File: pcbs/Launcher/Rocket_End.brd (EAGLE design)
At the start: 100 x 80 mm, 28 parts, among them IC1 7805TV, K4 LD105, K5 LD105, K6 LD105, K7 LD105, T1 BC547, T2 BC547, T3 BC547, T4 BC547, T5 BC547, U1 ARDUINO-MEGAPRO-5V, X1 22-23-2041, X2 22-23-2041, X4 22-23-2021, X5 22-23-2021, X6 22-23-2021

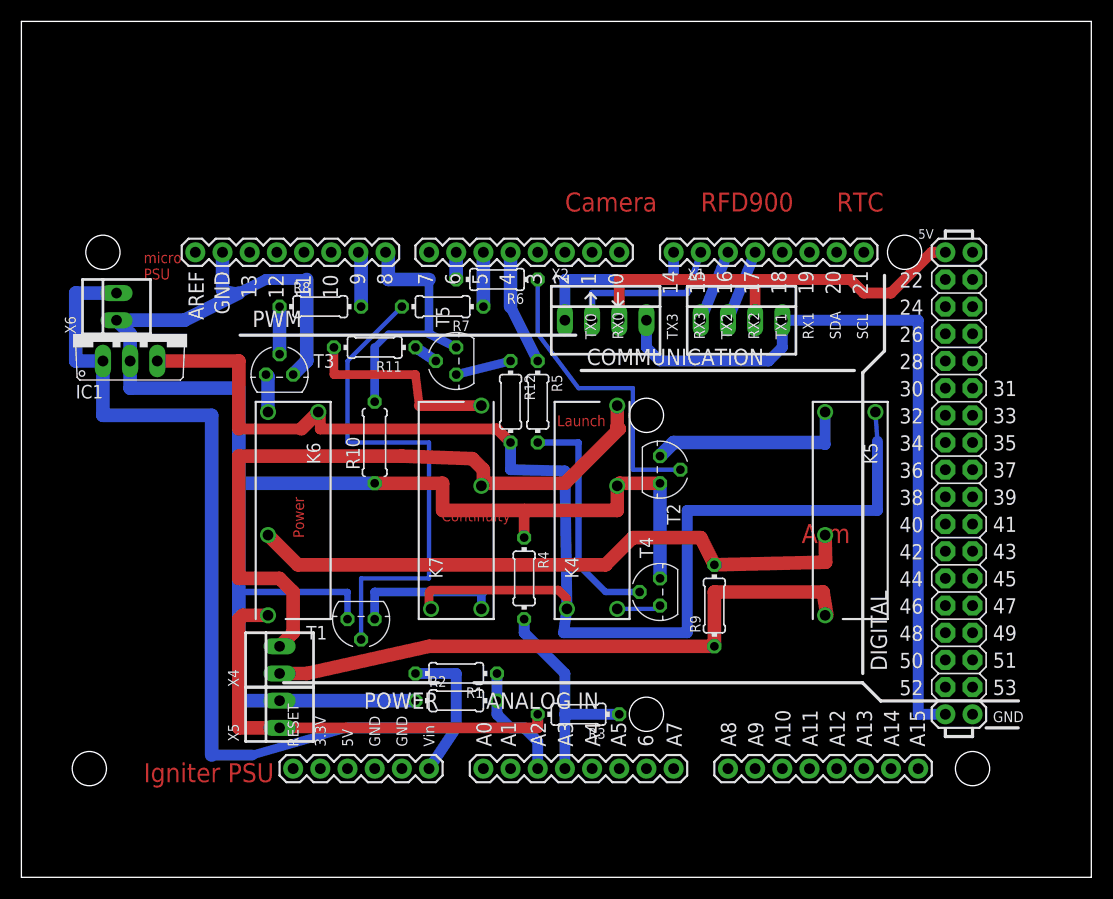
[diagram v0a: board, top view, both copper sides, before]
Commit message: * Much better placement of components and tracks for Rocket_End * Put IMU on bottom of the Sensor board
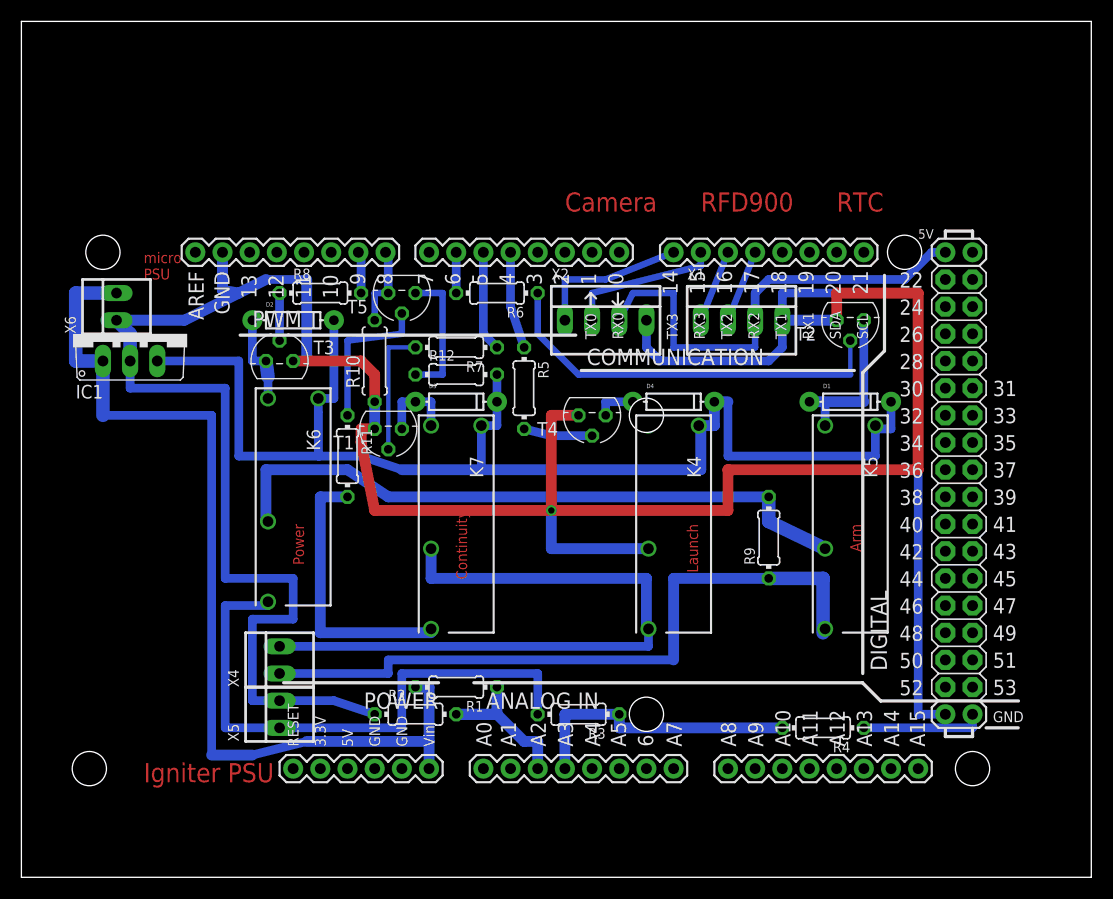
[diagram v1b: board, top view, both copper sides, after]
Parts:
- added D1, D2, D3, D4: (no value), SparkFun-DiscreteSemi:DIODE-1N4148
- moved R4 31.2 mm to (74.9, 14.0), turned to 180 degrees
- moved T2 22.6 mm to (77.5, 52.1), turned to 180 degrees
- moved T1 18.0 mm to (34.3, 41.9)
- moved T4 17.7 mm to (53.3, 43.2), turned to 180 degrees
- moved R11 10.5 mm to (30.5, 39.4), turned to 270 degrees
- moved R9 8.13 mm to (69.8, 31.8)
- moved T5 8.13 mm to (35.6, 54.6), turned to 180 degrees
- moved K4 7.73 mm to (61.0, 33.0), turned to 270 degrees
- moved R10 7.62 mm to (33.0, 48.3)
- moved R12 5.68 mm to (40.6, 47.0), turned to 0 degrees
- moved R7 4.02 mm to (40.6, 49.5)
- moved R2 4.02 mm to (36.8, 15.2)
- moved R5 1.80 mm to (47.0, 45.7)
- moved K6 1.27 mm to (25.4, 35.6)
- moved R6 1.27 mm to (44.5, 54.6)
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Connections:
- new net N$24: R4.1, U1.GND@3
- net GND: no longer R4.1
- net N$19: now also D4.A
- net N$20: now also D3.A
- net N$21: now also D2.A
- net N$22: now also D1.A
- net N$5: now also D1.C, D2.C, D3.C, D4.C
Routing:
- net GND: track 164.4 -> 233.4 mm
- net N$13: track 47.2 -> 12.1 mm
- net N$26: track 25.1 -> 7.87 mm
- net N$12: track 22.0 -> 6.43 mm
- net N$31: track 2.29 -> 14.0 mm
- net N$29: track 42.2 -> 53.9 mm
- net N$24: track 0.00 -> 11.4 mm
- net N$10: track 28.6 -> 37.8 mm
- net N$23: track 5.24 -> 12.7 mm
- net VCC: track 96.4 -> 89.1 mm
- net N$30: track 18.9 -> 25.9 mm
- net N$20: track 14.4 -> 7.50 mm
- net N$17: track 58.4 -> 64.8 mm
- net N$7: track 11.2 -> 17.6 mm
- net N$3: track 20.6 -> 26.7 mm
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
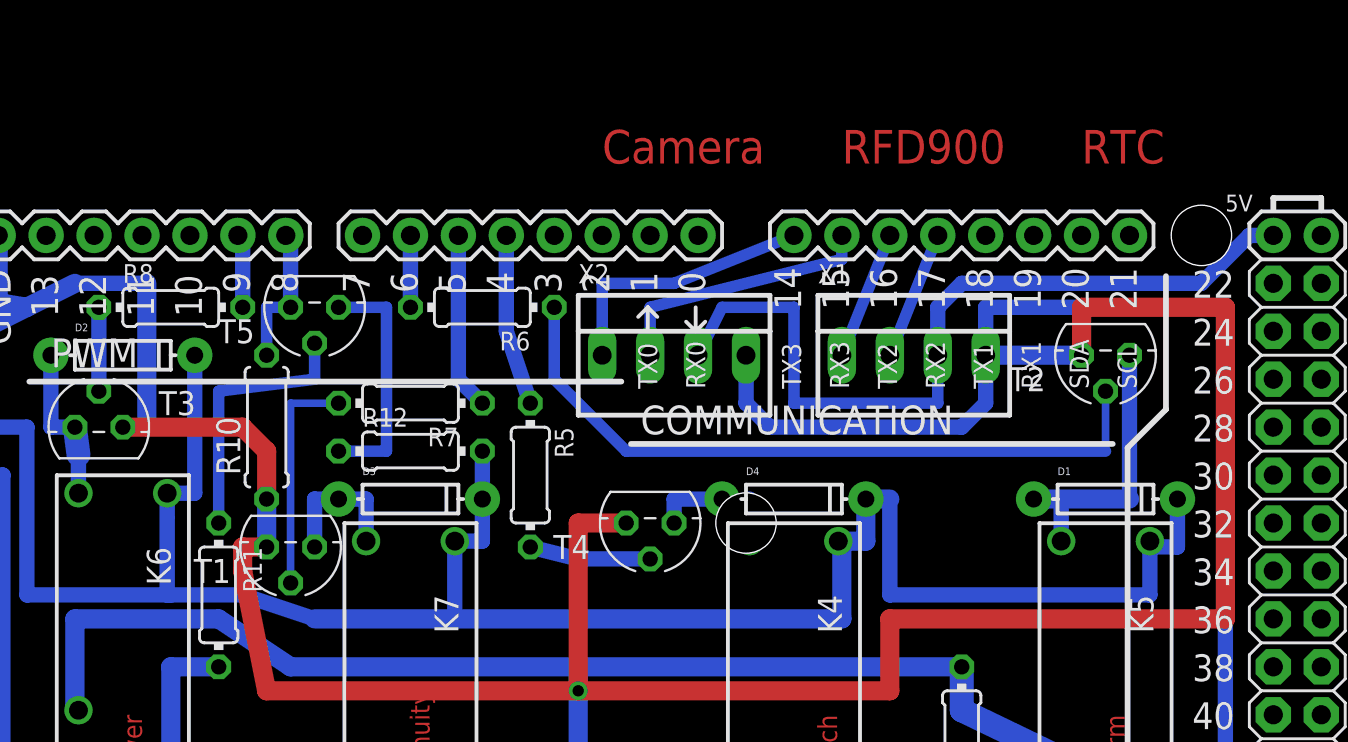
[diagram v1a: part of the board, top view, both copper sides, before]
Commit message: * Using Via to ensure soldering is done on correct side of board.
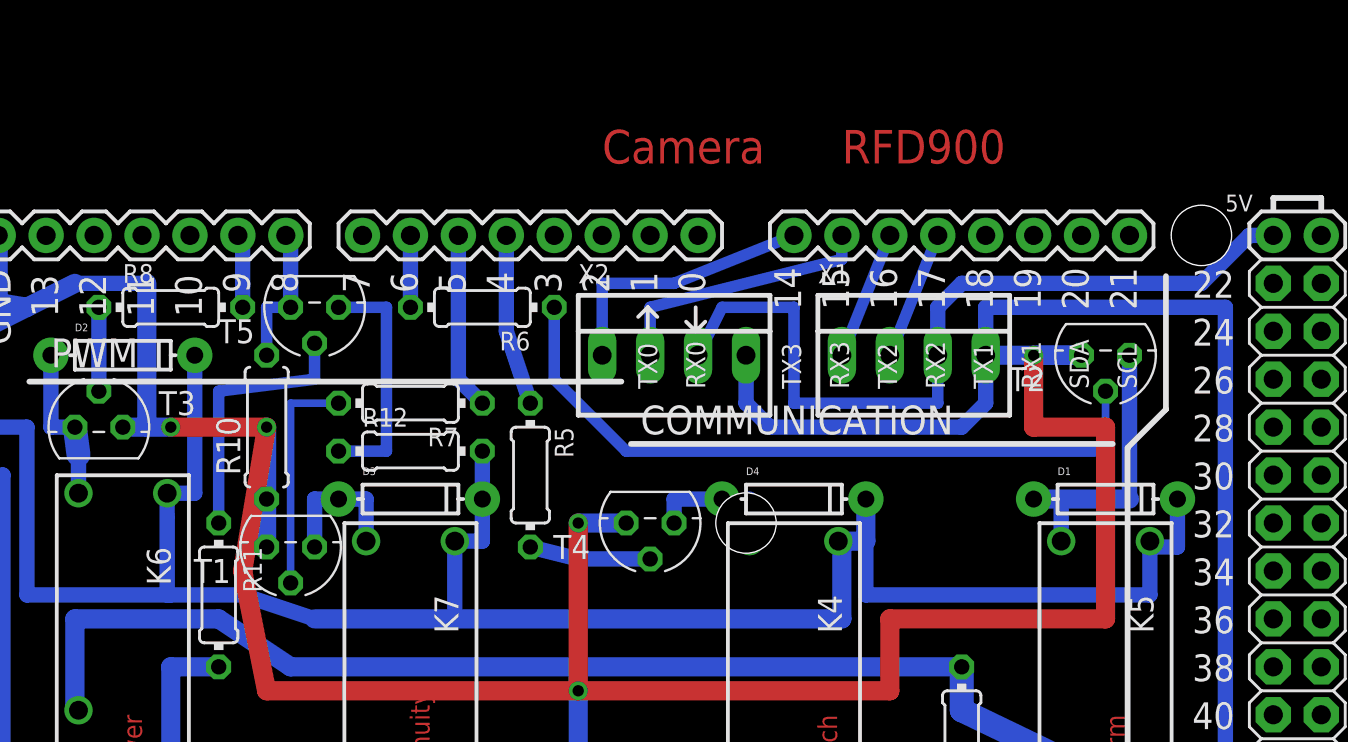
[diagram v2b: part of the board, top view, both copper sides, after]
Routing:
- net GND: track 233.4 -> 226.6 mm, vias 0 -> 4
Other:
- board text removed: "RTC"
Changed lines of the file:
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@@
 <wire x1="100" y1="80" x2="0" y2="80" width="0" layer="20"/>
 <wire x1="0" y1="80" x2="0" y2="0" width="0" layer="20"/>
-<text x="76.2" y="62.23" size="1.778" layer="1">RTC</text>
 <text x="50.8" y="62.23" size="1.778" layer="1">Camera</text>
 <text x="63.5" y="62.23" size="1.778" layer="1">RFD900</text>
@@
 <contactref element="R2" pad="1"/>
 <wire x1="33.02" y1="15.24" x2="29.21" y2="16.51" width="0.8128" layer="16"/>
-<wire x1="33.02" y1="44.45" x2="33.02" y2="46.99" width="1.016" layer="1"/>
-<wire x1="33.02" y1="46.99" x2="31.75" y2="48.26" width="1.016" layer="1"/>
-<wire x1="31.75" y1="48.26" x2="25.4" y2="48.26" width="1.016" layer="1"/>
-<wire x1="33.02" y1="41.91" x2="31.75" y2="41.91" width="1.016" layer="1"/>
-<wire x1="31.75" y1="41.91" x2="31.75" y2="40.64" width="1.016" layer="1"/>
+<wire x1="33.02" y1="44.45" x2="33.02" y2="48.26" width="1.016" layer="16"/>
+<wire x1="33.02" y1="48.26" x2="27.94" y2="48.26" width="1.016" layer="1"/>
+<wire x1="27.94" y1="48.26" x2="25.4" y2="48.26" width="1.016" layer="16"/>
+<wire x1="33.02" y1="41.91" x2="33.02" y2="48.26" width="0" layer="19" extent="1-16"/>
+<wire x1="33.02" y1="48.26" x2="31.75" y2="40.64" width="1.016" layer="1"/>
 <wire x1="31.75" y1="40.64" x2="33.02" y2="34.29" width="1.016" layer="1"/>
 <wire x1="33.02" y1="34.29" x2="49.53" y2="34.29" width="1.016" layer="1"/>
 <wire x1="49.53" y1="34.29" x2="49.53" y2="43.18" width="1.016" layer="1"/>
-<wire x1="49.53" y1="43.18" x2="52.07" y2="43.18" width="1.016" layer="1"/>
+<wire x1="49.53" y1="43.18" x2="52.07" y2="43.18" width="1.016" layer="16"/>
 <wire x1="58.61" y1="30.72" x2="49.53" y2="30.72" width="1.016" layer="16"/>
 <wire x1="49.53" y1="30.72" x2="49.53" y2="35.56" width="1.016" layer="16"/>
@@
 <wire x1="49.53" y1="34.29" x2="66.04" y2="34.29" width="1.016" layer="1"/>
 <wire x1="66.04" y1="34.29" x2="66.04" y2="38.1" width="1.016" layer="1"/>
-<wire x1="66.04" y1="38.1" x2="83.82" y2="38.1" width="1.016" layer="1"/>
+<wire x1="66.04" y1="38.1" x2="77.47" y2="38.1" width="1.016" layer="1"/>
 <wire x1="76.2" y1="52.07" x2="71.12" y2="52.07" width="1.016" layer="16"/>
-<wire x1="83.82" y1="38.1" x2="83.82" y2="54.61" width="1.016" layer="1"/>
-<wire x1="83.82" y1="54.61" x2="76.2" y2="54.61" width="1.016" layer="1"/>
-<wire x1="76.2" y1="54.61" x2="76.2" y2="52.07" width="1.016" layer="1"/>
+<wire x1="77.47" y1="38.1" x2="77.47" y2="48.26" width="1.016" layer="1"/>
+<wire x1="77.47" y1="48.26" x2="73.66" y2="48.26" width="1.016" layer="1"/>
+<wire x1="73.66" y1="48.26" x2="73.66" y2="52.07" width="1.016" layer="1"/>
+<wire x1="73.66" y1="52.07" x2="76.2" y2="52.07" width="1.016" layer="16"/>
 <wire x1="49.53" y1="34.29" x2="49.53" y2="35.56" width="0" layer="19" extent="1-16"/>
+<via x="27.94" y="48.26" extent="1-16" drill="0.6" shape="square"/>
+<via x="33.02" y="48.26" extent="1-16" drill="0.6" shape="square"/>
+<wire x1="33.02" y1="48.26" x2="31.75" y2="41.91" width="0" layer="19" extent="1-16"/>
+<via x="49.53" y="43.18" extent="1-16" drill="0.6" shape="square"/>
+<via x="73.66" y="52.07" extent="1-16" drill="0.6" shape="square"/>
 </signal>
 <signal name="VCC">
@@
 <wire x1="63.5" y1="42.22" x2="64.77" y2="42.22" width="1.016" layer="16"/>
 <wire x1="64.77" y1="42.22" x2="64.77" y2="44.45" width="1.016" layer="16"/>
-<wire x1="64.77" y1="44.45" x2="66.04" y2="44.45" width="1.016" layer="16"/>
-<wire x1="66.04" y1="44.45" x2="66.04" y2="39.37" width="0.8128" layer="16"/>
-<wire x1="66.04" y1="39.37" x2="79.82" y2="39.37" width="0.8128" layer="16"/>
+<wire x1="64.77" y1="44.45" x2="64.77" y2="39.37" width="0.8128" layer="16"/>
+<wire x1="64.77" y1="39.37" x2="79.82" y2="39.37" width="0.8128" layer="16"/>
 <wire x1="79.82" y1="39.37" x2="79.82" y2="42.22" width="0.8128" layer="16"/>
 <wire x1="42.99" y1="42.22" x2="44.45" y2="42.22" width="0.8128" layer="16"/>

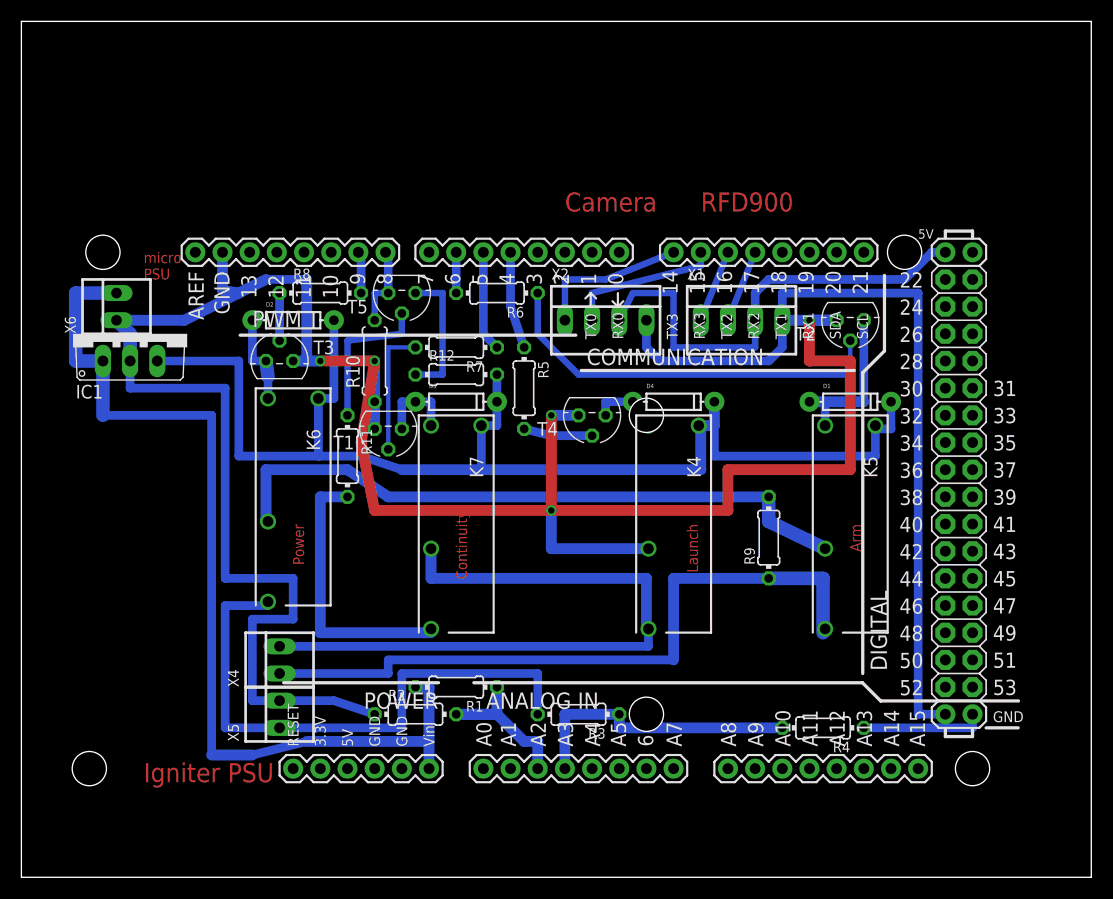
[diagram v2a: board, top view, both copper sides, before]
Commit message: * More mods....fixed up gps wiring. * Making place where can run some wires underneath so don't need   two sides for relay board.
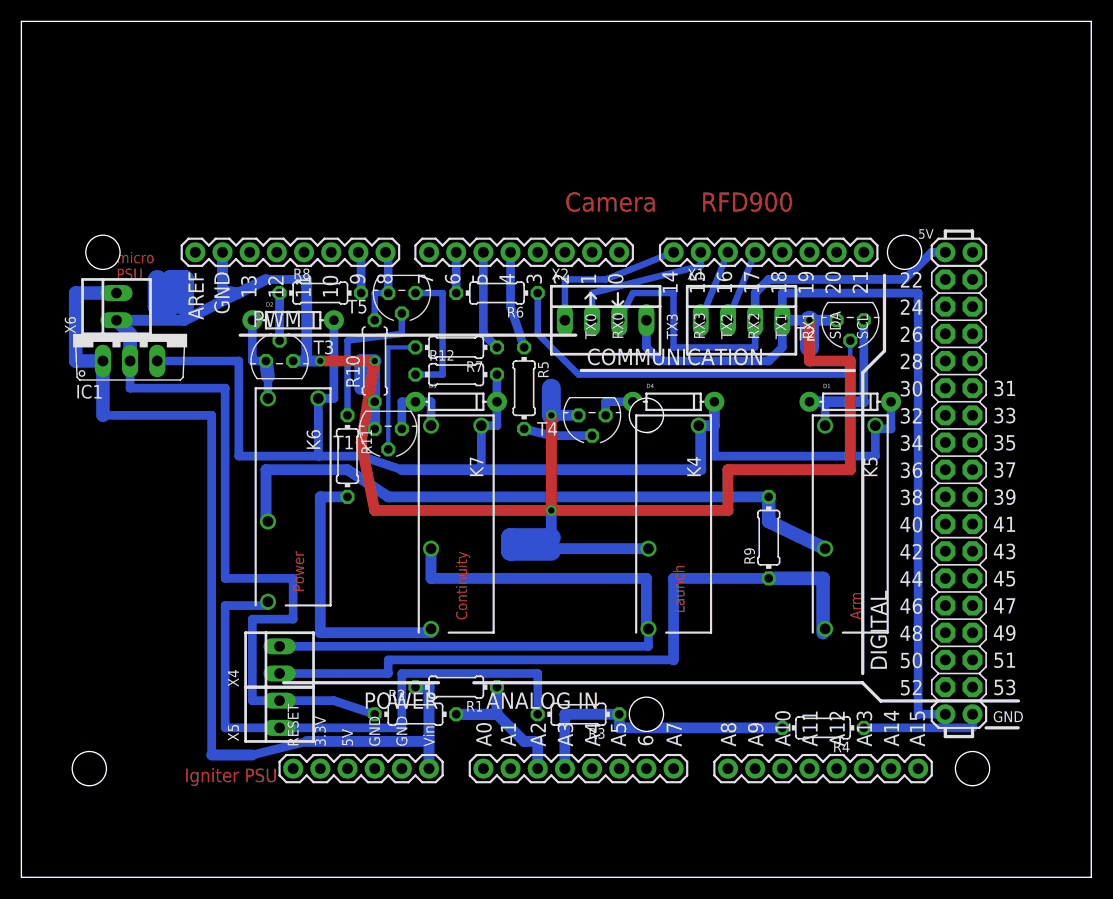
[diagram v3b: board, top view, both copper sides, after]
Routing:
- net GND: track 226.6 -> 241.9 mm
- net N$33: track 0.00 -> 10.2 mm
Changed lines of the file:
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@@
 <text x="50.8" y="62.23" size="1.778" layer="1">Camera</text>
 <text x="63.5" y="62.23" size="1.778" layer="1">RFD900</text>
-<text x="25.4" y="33.02" size="1.016" layer="1" rot="R270">Power</text>
-<text x="77.47" y="33.02" size="1.016" layer="1" rot="R270">Arm</text>
-<text x="62.23" y="33.02" size="1.016" layer="1" rot="R270">Launch</text>
-<text x="40.64" y="34.29" size="1.016" layer="1" rot="R270">Continuity</text>
-<text x="11.43" y="8.89" size="1.778" layer="1">Igniter PSU</text>
-<text x="11.43" y="55.88" size="1.016" layer="1">micro
+<text x="25.4" y="30.48" size="1.016" layer="1" rot="R270">Power</text>
+<text x="77.47" y="26.67" size="1.016" layer="1" rot="R270">Arm</text>
+<text x="60.96" y="29.21" size="1.016" layer="1" rot="R270">Launch</text>
+<text x="40.64" y="30.48" size="1.016" layer="1" rot="R270">Continuity</text>
+<text x="15.24" y="8.89" size="1.27" layer="1">Igniter PSU</text>
+<text x="8.89" y="55.88" size="1.016" layer="1">micro
 PSU</text>
 </plain>
@@
 <wire x1="49.53" y1="43.18" x2="52.07" y2="43.18" width="1.016" layer="16"/>
 <wire x1="58.61" y1="30.72" x2="49.53" y2="30.72" width="1.016" layer="16"/>
-<wire x1="49.53" y1="30.72" x2="49.53" y2="35.56" width="1.016" layer="16"/>
+<wire x1="49.53" y1="30.72" x2="49.53" y2="31.75" width="1.016" layer="16"/>
+<wire x1="49.53" y1="31.75" x2="49.53" y2="35.56" width="1.016" layer="16"/>
 <wire x1="24.13" y1="16.51" x2="21.59" y2="16.51" width="0.8128" layer="16"/>
 <wire x1="21.59" y1="16.51" x2="21.59" y2="24.13" width="0.8128" layer="16"/>
@@
 <wire x1="66.04" y1="34.29" x2="66.04" y2="38.1" width="1.016" layer="1"/>
 <wire x1="66.04" y1="38.1" x2="77.47" y2="38.1" width="1.016" layer="1"/>
-<wire x1="76.2" y1="52.07" x2="71.12" y2="52.07" width="1.016" layer="16"/>
+<wire x1="73.66" y1="52.07" x2="71.12" y2="52.07" width="1.016" layer="16"/>
 <wire x1="77.47" y1="38.1" x2="77.47" y2="48.26" width="1.016" layer="1"/>
 <wire x1="77.47" y1="48.26" x2="73.66" y2="48.26" width="1.016" layer="1"/>
@@
 <via x="49.53" y="43.18" extent="1-16" drill="0.6" shape="square"/>
 <via x="73.66" y="52.07" extent="1-16" drill="0.6" shape="square"/>
+<wire x1="49.53" y1="43.18" x2="49.53" y2="45.72" width="1.778" layer="16"/>
+<wire x1="73.66" y1="52.07" x2="73.66" y2="49.53" width="1.778" layer="16"/>
+<wire x1="49.53" y1="31.75" x2="45.72" y2="31.75" width="1.778" layer="16"/>
+<wire x1="45.72" y1="31.75" x2="45.72" y2="30.48" width="1.778" layer="16"/>
+<wire x1="45.72" y1="30.48" x2="49.53" y2="30.48" width="1.778" layer="16"/>
+<wire x1="33.02" y1="48.26" x2="31.75" y2="48.26" width="1.27" layer="16"/>
+<wire x1="31.75" y1="48.26" x2="31.75" y2="45.72" width="1.27" layer="16"/>
 </signal>
 <signal name="VCC">
@@
 <via x="49.53" y="34.29" extent="1-16" drill="0.6" shape="square"/>
 </signal>
+<signal name="N$33">
+<wire x1="12.7" y1="55.88" x2="12.7" y2="53.34" width="1.778" layer="16"/>
+<wire x1="12.7" y1="53.34" x2="13.97" y2="53.34" width="1.778" layer="16"/>
+<wire x1="13.97" y1="53.34" x2="13.97" y2="55.88" width="1.778" layer="16"/>
+<wire x1="13.97" y1="55.88" x2="15.24" y2="55.88" width="1.778" layer="16"/>
+<wire x1="15.24" y1="55.88" x2="15.24" y2="53.34" width="1.778" layer="16"/>
+</signal>
 </signals>
